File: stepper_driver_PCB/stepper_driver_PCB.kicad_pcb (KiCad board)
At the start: 4 copper layers, 42.3 x 42.3 mm, 13 parts, among them J1 POWER, J2 JTAG, J3 CTRL, J4 STEPPER, U1 STM32F411CEUx, U2 TMC2226-SA, U5 24LC512

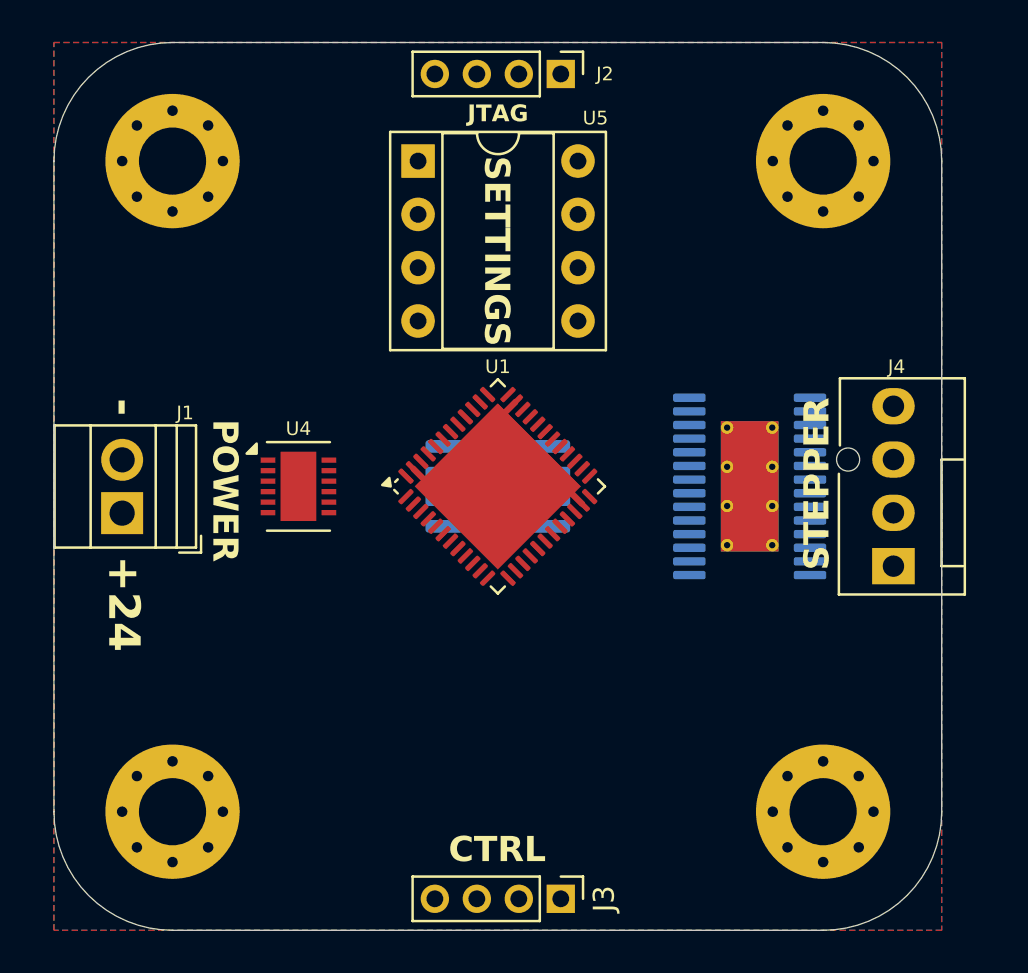
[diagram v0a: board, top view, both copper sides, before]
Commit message: Added .gitignore and placed essential parts
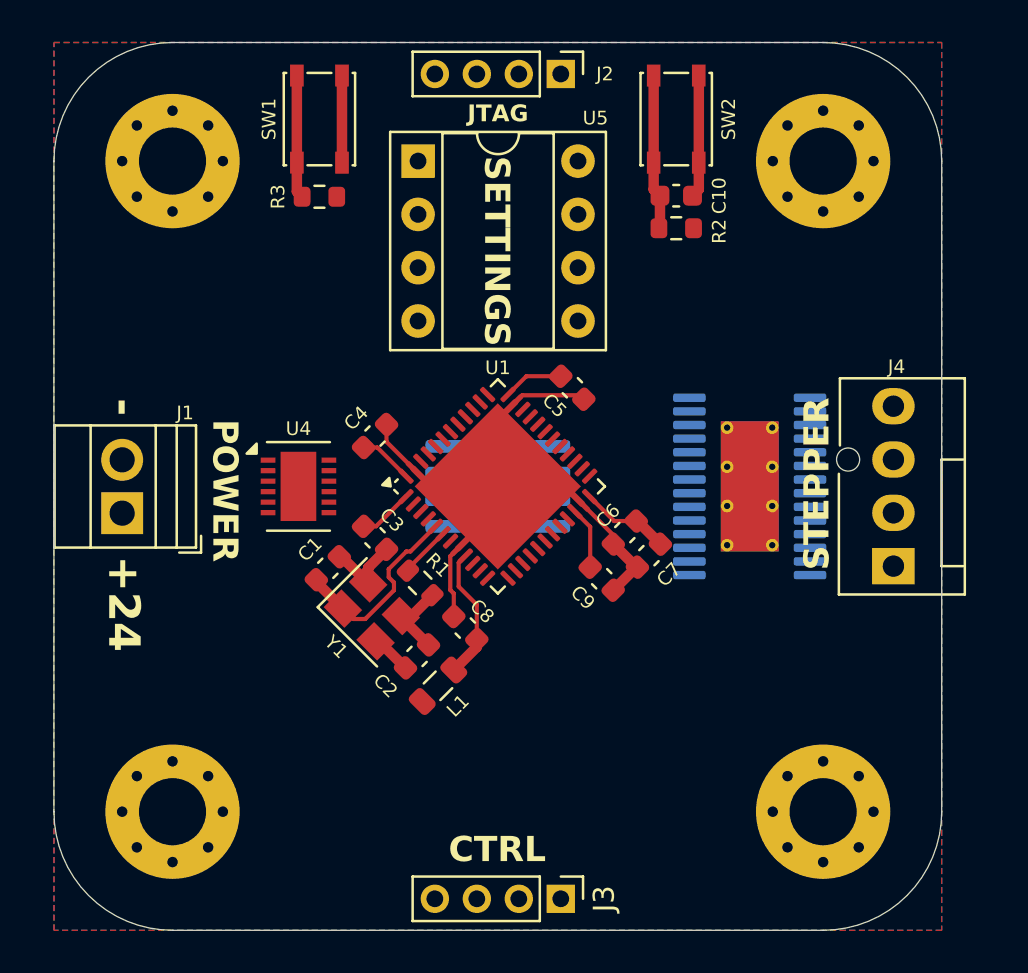
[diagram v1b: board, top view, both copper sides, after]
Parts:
- added C1: 12p, Capacitor_SMD:C_0603_1608Metric, F.Cu at (107.4, 99.4)
- added C10: 100n, Capacitor_SMD:C_0603_1608Metric, F.Cu at (124.0, 81.7)
- added C2: 12p, Capacitor_SMD:C_0603_1608Metric, F.Cu at (111.7, 103.6)
- added C3: 100n, Capacitor_SMD:C_0603_1608Metric, F.Cu at (109.7, 98.0)
- added C4: 100n, Capacitor_SMD:C_0603_1608Metric, F.Cu at (109.7, 93.1)
- added C5: 100n, Capacitor_SMD:C_0603_1608Metric, F.Cu at (119.0, 90.8)
- added C6: 100n, Capacitor_SMD:C_0603_1608Metric, F.Cu at (121.5, 97.7)
- added C7: 4u7, Capacitor_SMD:C_0603_1608Metric, F.Cu at (122.7, 98.8)
- added C8: 100n, Capacitor_SMD:C_0603_1608Metric, F.Cu at (114.0, 102.2)
- added C9: 2u2, Capacitor_SMD:C_0603_1608Metric, F.Cu at (120.5, 99.9)
- added L1: 10u, Inductor_SMD:L_0805_2012Metric, F.Cu at (112.7, 105.0)
- added R1: 47, Resistor_SMD:R_0603_1608Metric, F.Cu at (111.8, 100.1)
- added R2: 10k, Resistor_SMD:R_0603_1608Metric, F.Cu at (124.0, 83.2)
- added R3: 10k, Resistor_SMD:R_0603_1608Metric, F.Cu at (107.0, 81.7)
- added SW1: BTN, Button_Switch_SMD:SW_SPST_PTS810, F.Cu at (107.0, 78.0)
- added SW2: BTN, Button_Switch_SMD:SW_SPST_PTS810, F.Cu at (124.0, 78.0)
- added Y1: 25MHz, Crystal:Crystal_SMD_3225-4Pin_3.2x2.5mm, F.Cu at (109.5, 101.5)
- U1: value STM32F411CEUx -> STM32F412CEUx
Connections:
- U1 pad 1: unconnected-(U1-VBAT-Pad1) -> +3.3V
- U1 pad 22: unconnected-(U1-VCAP1-Pad22) -> Net-(U1-VCAP_1)
- U1 pad 23: Net-(U1-VSS-Pad23) -> GND
- U1 pad 24: unconnected-(U1-VDD-Pad24) -> +3.3V
- U1 pad 35: Net-(U1-VSS-Pad23) -> GND
- U1 pad 36: unconnected-(U1-VDD-Pad36) -> +3.3V
- U1 pad 47: Net-(U1-VSS-Pad23) -> GND
- U1 pad 48: unconnected-(U1-VDD-Pad48) -> +3.3V
- U1 pad 49: Net-(U1-VSS-Pad23) -> GND
- U1 pad 5: unconnected-(U1-PH0-Pad5) -> /HSE_IN
- U1 pad 6: unconnected-(U1-PH1-Pad6) -> /HSE_OUT
- U1 pad 8: unconnected-(U1-VSSA-Pad8) -> GND
- U1 pad 9: unconnected-(U1-VDDA-Pad9) -> +3.3VA
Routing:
- net GND: track 0.00 -> 43.8 mm
- net Net-(U1-VSS-Pad23): track 13.1 -> 0.00 mm
- net +3.3V: track 0.00 -> 12.4 mm
- net /HSE_IN: track 0.00 -> 9.30 mm
- net /NRST: track 0.00 -> 7.42 mm
- net +3.3VA: track 0.00 -> 6.38 mm
- net /BOOT0: track 0.00 -> 5.88 mm
- net +3V3: track 0.00 -> 4.15 mm
- net Net-(C2-Pad1): track 0.00 -> 3.84 mm
- net Net-(U1-VCAP_1): track 0.00 -> 2.96 mm
- net /HSE_OUT: track 0.00 -> 2.46 mm

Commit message: Added USB port for configuration and testing
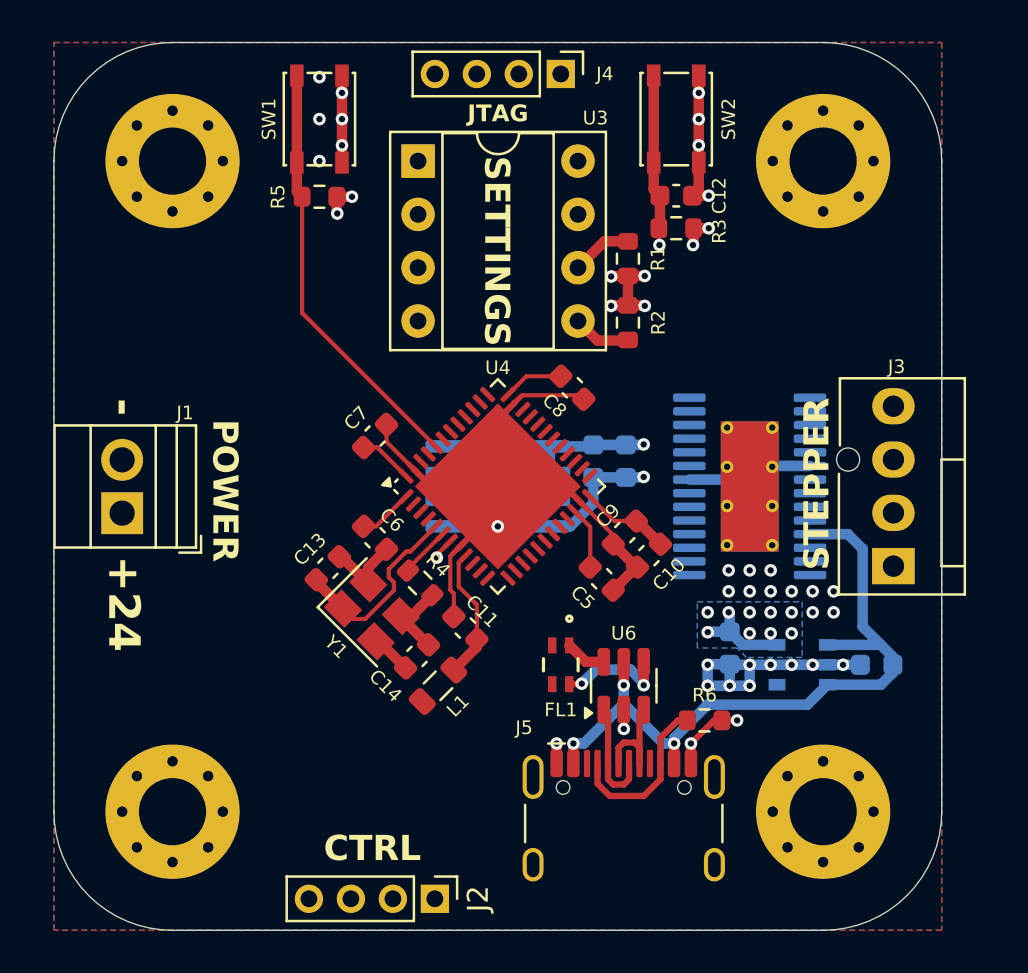
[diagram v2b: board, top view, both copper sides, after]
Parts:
- removed the U3 at (115.5, 95.5)
- removed the U4 at (106.0, 95.5)
- added C1: 1u, Capacitor_SMD:C_0603_1608Metric, B.Cu at (133.6, 104.0)
- added C2: 1u, Capacitor_SMD:C_0603_1608Metric, B.Cu at (126.6, 103.2)
- added C3: 100n, Capacitor_SMD:C_0603_1608Metric, B.Cu at (120.0, 94.3)
- added C4: 1u, Capacitor_SMD:C_0603_1608Metric, B.Cu at (121.6, 94.3)
- added FL1: TDK ACM2012-900, ACM2012_900_2P_T002:ACM2012_TDK, F.Cu at (118.5, 104.0)
- added J5: USB-C 16P, Connector_USB:USB_C_Receptacle_HCTL_HC-TYPE-C-16P-01A, F.Cu at (121.5, 112.5)
- added R1: 2k2, Resistor_SMD:R_0603_1608Metric, F.Cu at (121.7, 84.7)
- added R2: 2k2, Resistor_SMD:R_0603_1608Metric, F.Cu at (121.7, 87.7)
- added R6: 5k1, Resistor_SMD:R_0603_1608Metric, F.Cu at (125.3, 106.7)
- added U1: AP7343, Custom:SOT-25, B.Cu at (130.0, 104.0)
- added U2: ~, Package_SO:SOIC-8_3.9x4.9mm_P1.27mm, B.Cu at (115.5, 95.5)
- added U6: USBLC6-2SC6, Package_TO_SOT_SMD:SOT-23-6, F.Cu at (121.5, 105.0)
- moved J2 6.00 mm to (112.5, 115.2)
- renumbered C7 to C10, C8 to C11, C10 to C12, C1 to C13, C2 to C14, C9 to C5, C3 to C6, C4 to C7, C5 to C8, C6 to C9, J3 to J2, J4 to J3, J2 to J4, R2 to R3, R1 to R4, R3 to R5, U5 to U3, U1 to U4, U2 to U5
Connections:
- J3 pad 1: unconnected-(J4-Pin_1-Pad1) (its old number) -> /STEPPER_A2
- J3 pad 2: unconnected-(J4-Pin_2-Pad2) (its old number) -> /STEPPER_A1
- J3 pad 3: unconnected-(J4-Pin_3-Pad3) (its old number) -> /STEPPER_B2
- J3 pad 4: unconnected-(J4-Pin_4-Pad4) (its old number) -> /STEPPER_B1
- U3 pad 1: unconnected-(U5-A0-Pad1) -> GND
- U3 pad 2: unconnected-(U5-A1-Pad2) -> GND
- U3 pad 3: unconnected-(U5-A2-Pad3) -> GND
- U3 pad 4: unconnected-(U5-GND-Pad4) -> GND
- U3 pad 5: unconnected-(U5-SDA-Pad5) -> /SDA
- U3 pad 6: unconnected-(U5-SCL-Pad6) -> /SCL
- U3 pad 7: unconnected-(U5-WP-Pad7) -> /24LC512_WP
- U3 pad 8: unconnected-(U5-VCC-Pad8) -> +3V3
- U4 pad 44: unconnected-(U1-BOOT0-Pad44) -> /BOOT0
- U4 pad 7: unconnected-(U1-NRST-Pad7) -> /NRST
- U5 pad 1: unconnected-(U2-OB1-Pad1) -> /STEPPER_B1
- U5 pad 11: unconnected-(U2-5VOUT-Pad11) -> +5V
- U5 pad 19: unconnected-(U2-VCC_IO-Pad19) -> +3.3V
- U5 pad 25: unconnected-(U2-OA2-Pad25) -> /STEPPER_A2
- U5 pad 28: unconnected-(U2-OA1-Pad28) -> /STEPPER_A1
- U5 pad 4: unconnected-(U2-OB2-Pad4) -> /STEPPER_B2
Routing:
- net +5V: track 0.00 -> 34.1 mm, vias 0 -> 3
- net GND: track 43.8 -> 70.1 mm, vias 0 -> 35
- net /NRST: track 7.42 -> 28.6 mm, vias 0 -> 2
- net +3V3: track 4.15 -> 20.6 mm, vias 0 -> 19
- net /BOOT0: track 5.88 -> 20.4 mm
- net Net-(J5-CC1): track 0.00 -> 8.13 mm
- net Net-(J5-D--PadA7): track 0.00 -> 5.36 mm
- net Net-(J5-D+-PadA6): track 0.00 -> 5.36 mm
- net /USB/FL_P: track 0.00 -> 5.32 mm, vias 0 -> 2
- net Net-(U5-GND-Pad22): track 0.00 -> 4.83 mm
- net /SCL: track 0.00 -> 2.90 mm
- net /SDA: track 0.00 -> 2.77 mm
- net /USB/FL_N: track 0.00 -> 1.97 mm
- added copper zone on B.Cu, net +3V3
- added copper zone on In2.Cu, net +3V3
- removed copper zone on In2.Cu, net GND
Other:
- board text added: "B1 B2 A1 A2"

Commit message: Layout
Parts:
- added C15: 22n/50v, Capacitor_SMD:C_0603_1608Metric, F.Cu at (130.3, 95.5)
- added C16: 100n/50v, Capacitor_SMD:C_0603_1608Metric, F.Cu at (127.5, 91.1)
- added D1: PWR, LED_SMD:LED_0603_1608Metric, F.Cu at (101.5, 105.1)
- added D2: STATUS, LED_SMD:LED_0603_1608Metric, F.Cu at (101.5, 103.5)
- added R10: 2k2, Resistor_SMD:R_0603_1608Metric, F.Cu at (130.3, 92.5)
- added R7: 5k1, Resistor_SMD:R_0603_1608Metric, F.Cu at (98.4, 105.1)
- added R8: 1k, Resistor_SMD:R_0603_1608Metric, F.Cu at (98.4, 103.5)
- added R9: 2k2, Resistor_SMD:R_0603_1608Metric, F.Cu at (121.7, 81.6)
- C5: value 2u2 -> 4u7
- moved J1 2.58 mm to (97.6, 94.2), turned to -90 degrees
- moved C8 1.17 mm to (118.2, 90.0), turned to 0 degrees
- moved J3 0.95 mm to (135.3, 99.2)
- moved C7 0.68 mm to (109.1, 93.5)
- moved C12 0.50 mm to (124.5, 81.7)
- moved R3 0.50 mm to (124.5, 83.2)
- moved R5 0.50 mm to (106.5, 81.7)
- moved SW1 0.50 mm to (106.5, 78.0)
- moved SW2 0.50 mm to (124.5, 78.0)
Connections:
- C10 pad 1: +3.3V -> +3V3
- C6 pad 1: +3.3V -> +3V3
- C7 pad 1: +3.3V -> +3V3
- C8 pad 1: +3.3V -> +3V3
- C9 pad 1: +3.3V -> +3V3
- J2 pad 1: unconnected-(J2-Pin_1-Pad1) -> /SPI_NCS
- J2 pad 2: unconnected-(J2-Pin_2-Pad2) -> /SPI_CLK
- J2 pad 3: unconnected-(J2-Pin_3-Pad3) -> /SPI_MISO
- J2 pad 4: unconnected-(J2-Pin_4-Pad4) -> /SPI_MOSI
- J4 pad 1: unconnected-(J4-Pin_1-Pad1) -> +3V3
- J4 pad 2: unconnected-(J4-Pin_2-Pad2) -> /JTAG_SWCLK
- J4 pad 3: unconnected-(J4-Pin_3-Pad3) -> /JTAG_SWDIO
- J4 pad 4: unconnected-(J4-Pin_4-Pad4) -> GND
- L1 pad 1: +3.3V -> +3V3
- U2 pad 6: /SCL -> /I2C_SCL
- U2 pad 7: /SDA -> /I2C_SDA
- U3 pad 5: /SDA -> /I2C_SDA
- U3 pad 6: /SCL -> /I2C_SCL
- U4 pad 1: +3.3V -> +3V3
- U4 pad 10: unconnected-(U4-PA0-Pad10) -> /AS5600_OUT
- U4 pad 14: unconnected-(U4-PA4-Pad14) -> /SPI_NCS
- U4 pad 15: unconnected-(U4-PA5-Pad15) -> /SPI_CLK
- U4 pad 16: unconnected-(U4-PA6-Pad16) -> /SPI_MISO
- U4 pad 17: unconnected-(U4-PA7-Pad17) -> /SPI_MOSI
- U4 pad 18: unconnected-(U4-PB0-Pad18) -> /TMC_STEP
- U4 pad 19: unconnected-(U4-PB1-Pad19) -> /TMC_DIR
- U4 pad 20: unconnected-(U4-PB2-Pad20) -> /TMC_MS1
- U4 pad 21: unconnected-(U4-PB10-Pad21) -> /I2C_SDA
- U4 pad 24: +3.3V -> +3V3
- U4 pad 31: unconnected-(U4-PA10-Pad31) -> /STATUS
- U4 pad 32: unconnected-(U4-PA11-Pad32) -> /USB_DN
- U4 pad 33: unconnected-(U4-PA12-Pad33) -> /USB_DP
- U4 pad 34: unconnected-(U4-PA13-Pad34) -> /JTAG_SWDIO
- U4 pad 36: +3.3V -> +3V3
- U4 pad 37: unconnected-(U4-PA14-Pad37) -> /JTAG_SWCLK
- U4 pad 38: unconnected-(U4-PA15-Pad38) -> /24LC512_WP
- U4 pad 39: unconnected-(U4-PB3-Pad39) -> /TMC_MS2
- U4 pad 40: unconnected-(U4-PB4-Pad40) -> /TMC_SPREAD
- U4 pad 41: unconnected-(U4-PB5-Pad41) -> /TMC_STDBY
- U4 pad 42: unconnected-(U4-PB6-Pad42) -> /TMC_NDP/UART
- U4 pad 43: unconnected-(U4-PB7-Pad43) -> /TMC_DIAG
- U4 pad 45: unconnected-(U4-PB8-Pad45) -> /TMC_NEN
- U4 pad 46: unconnected-(U4-PB9-Pad46) -> /I2C_SCL
- U4 pad 48: +3.3V -> +3V3
- U5 pad 10: unconnected-(U5-SPREAD-Pad10) -> /TMC_SPREAD
- U5 pad 12: unconnected-(U5-MS1_AD0-Pad12) -> /TMC_MS1
- U5 pad 14: unconnected-(U5-MS2_AD1-Pad14) -> /TMC_MS2
- U5 pad 15: unconnected-(U5-DIAG-Pad15) -> /TMC_DIAG
- U5 pad 17: unconnected-(U5-CLK-Pad17) -> GND
- U5 pad 18: unconnected-(U5-PDN_UART-Pad18) -> /TMC_NDP/UART
- U5 pad 19: +3.3V -> +3V3
- U5 pad 2: unconnected-(U5-BRB-Pad2) -> GND
- U5 pad 20: unconnected-(U5-STEP-Pad20) -> /TMC_STEP
- U5 pad 21: unconnected-(U5-VREF-Pad21) -> +3.3VA
- U5 pad 22: Net-(U5-GND-Pad22) -> GND
- U5 pad 23: unconnected-(U5-DIR-Pad23) -> /TMC_DIR
- U5 pad 24: unconnected-(U5-STDBY-Pad24) -> /TMC_STDBY
- U5 pad 27: unconnected-(U5-BRA-Pad27) -> GND
- U5 pad 29: Net-(U5-GND-Pad22) -> GND
- U5 pad 5: unconnected-(U5-~{EN}-Pad5) -> /TMC_NEN
- U5 pad 6: Net-(U5-GND-Pad22) -> GND
- U5 pad 7: unconnected-(U5-CPO-Pad7) -> Net-(U5-CPO)
- U5 pad 8: unconnected-(U5-CPI-Pad8) -> Net-(U5-CPI)
- U5 pad 9: unconnected-(U5-VCP-Pad9) -> Net-(U5-VCP)
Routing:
- net /TMC_MS2: track 0.00 -> 35.9 mm, vias 0 -> 3
- net +3V3: track 20.6 -> 54.2 mm, vias 19 -> 35
- net /TMC_SPREAD: track 0.00 -> 30.2 mm, vias 0 -> 3
- net /STATUS: track 0.00 -> 28.6 mm, vias 0 -> 2
- net /TMC_NEN: track 0.00 -> 28.0 mm, vias 0 -> 2
- net /TMC_STDBY: track 0.00 -> 27.7 mm, vias 0 -> 3
- net /TMC_NDP/UART: track 0.00 -> 27.5 mm, vias 0 -> 3
- net /TMC_DIAG: track 0.00 -> 27.3 mm, vias 0 -> 3
- net /SPI_MOSI: track 0.00 -> 24.0 mm, vias 0 -> 1
- net /SPI_MISO: track 0.00 -> 22.1 mm, vias 0 -> 1
- net /I2C_SDA: track 0.00 -> 21.1 mm, vias 0 -> 1
- net /SPI_CLK: track 0.00 -> 20.3 mm, vias 0 -> 1
- net /I2C_SCL: track 0.00 -> 18.3 mm, vias 0 -> 1
- net /USB_DP: track 0.00 -> 17.6 mm, vias 0 -> 2
- net /SPI_NCS: track 0.00 -> 17.4 mm
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- added copper zone on In2.Cu, net +24V
- added copper zone on F.Cu, net +3V3
